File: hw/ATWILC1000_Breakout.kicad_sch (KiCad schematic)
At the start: 1 part, among them IC1 ATWILC1000B-MU-Y

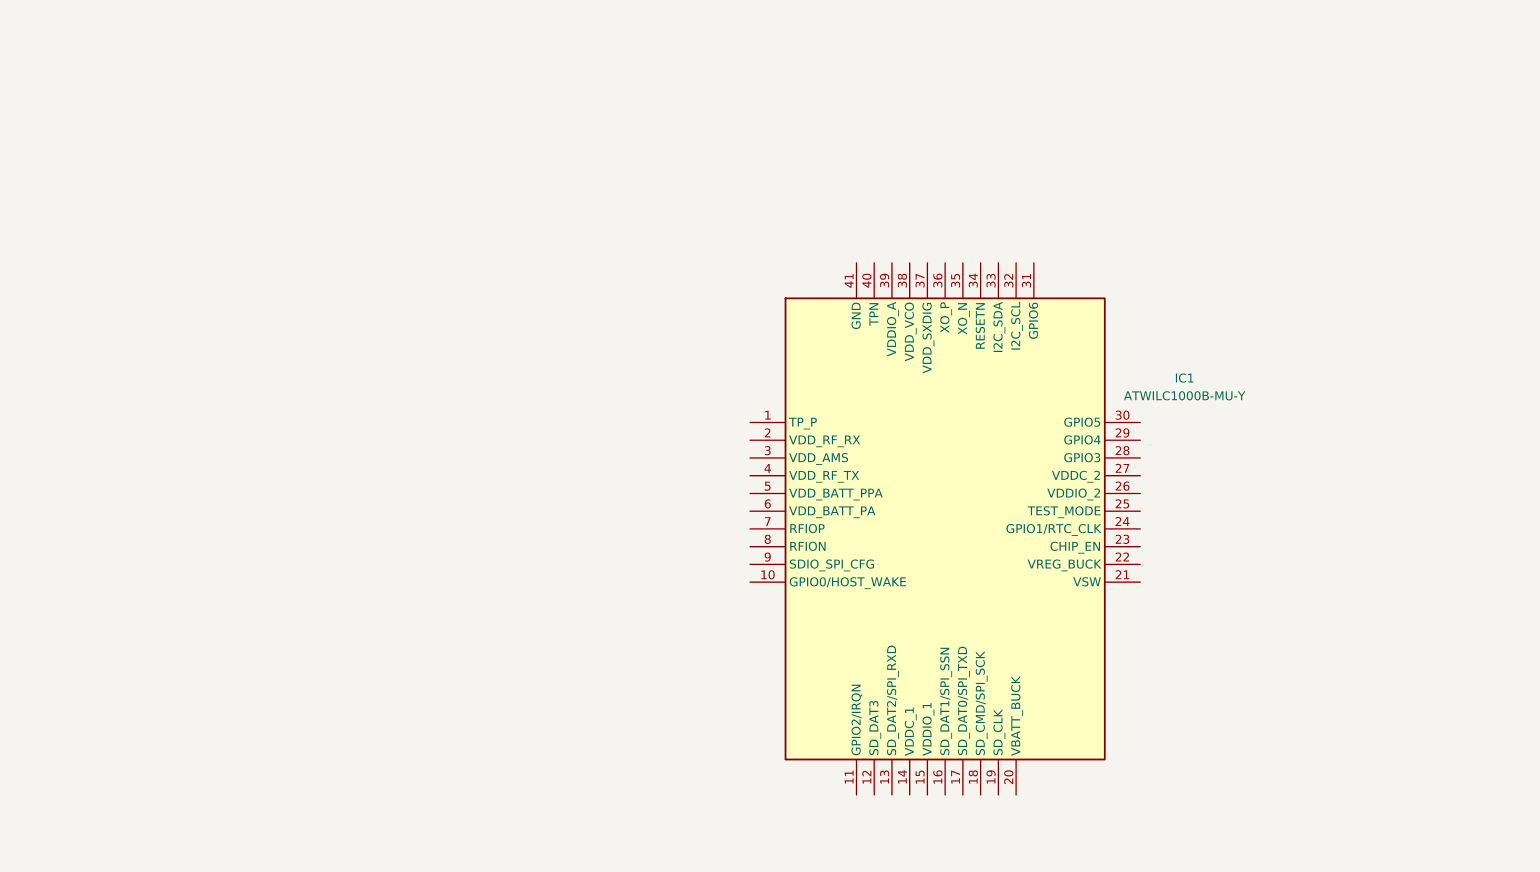
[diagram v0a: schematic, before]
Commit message: started initial power setup for breakout board
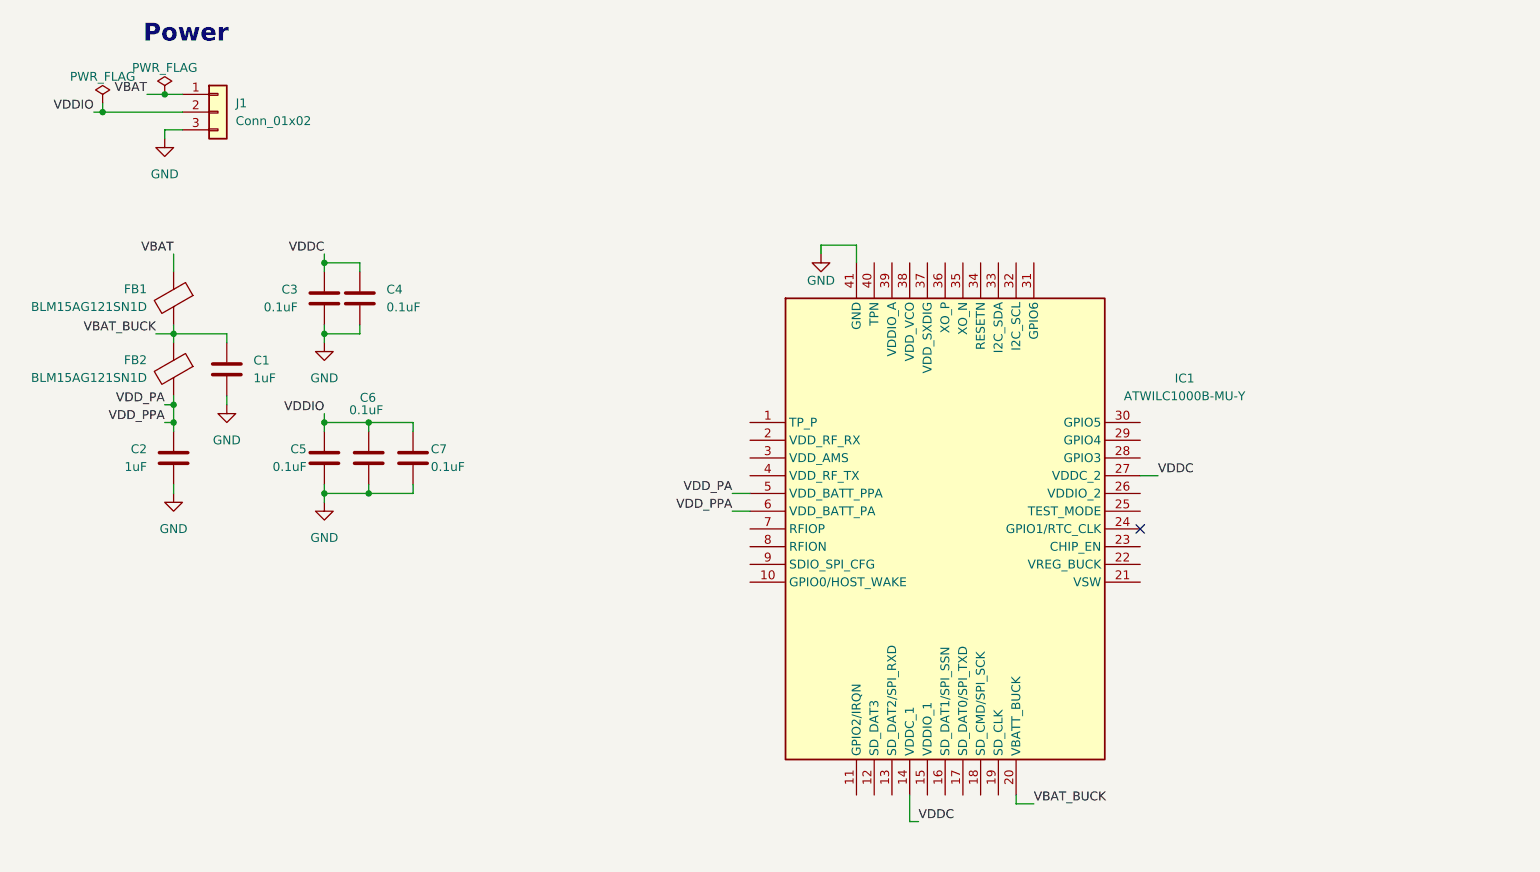
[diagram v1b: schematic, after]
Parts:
- added C1, C2: 1uF, symbol Device:C
- added C3, C4, C5, C6, C7: 0.1uF, symbol Device:C
- added FB1, FB2: BLM15AG121SN1D, symbol Device:FerriteBead
- added J1: Conn_01x02, symbol Connector_Generic:Conn_01x03
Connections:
- net VDDC: now reaches IC1.14 (VDDC_1)
- net VDDC: now also IC1.27 (VDDC_2), C3.1, C4.1
- net VBAT_BUCK: now reaches IC1.20 (VBATT_BUCK)
- net VBAT_BUCK: now also C1.1, FB1.2, FB2.1
- net GND: now reaches IC1.41 (GND)
- net GND: now also C1.2, C2.2, C3.2, C4.2, C5.2, C6.2, C7.2, J1.3 (Pin_3)
- net VDD_PA: now reaches IC1.5 (VDD_BATT_PPA)
- net VDD_PA: now also IC1.6 (VDD_BATT_PA), C2.1, FB2.2
- new net VBAT: FB1.1, J1.1 (Pin_1)
- new net VDDIO: C5.1, C6.1, C7.1, J1.2 (Pin_2)
- no-connect marks 0 -> 1
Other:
- note added: "Power"

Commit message: updated to the module rather than the chip
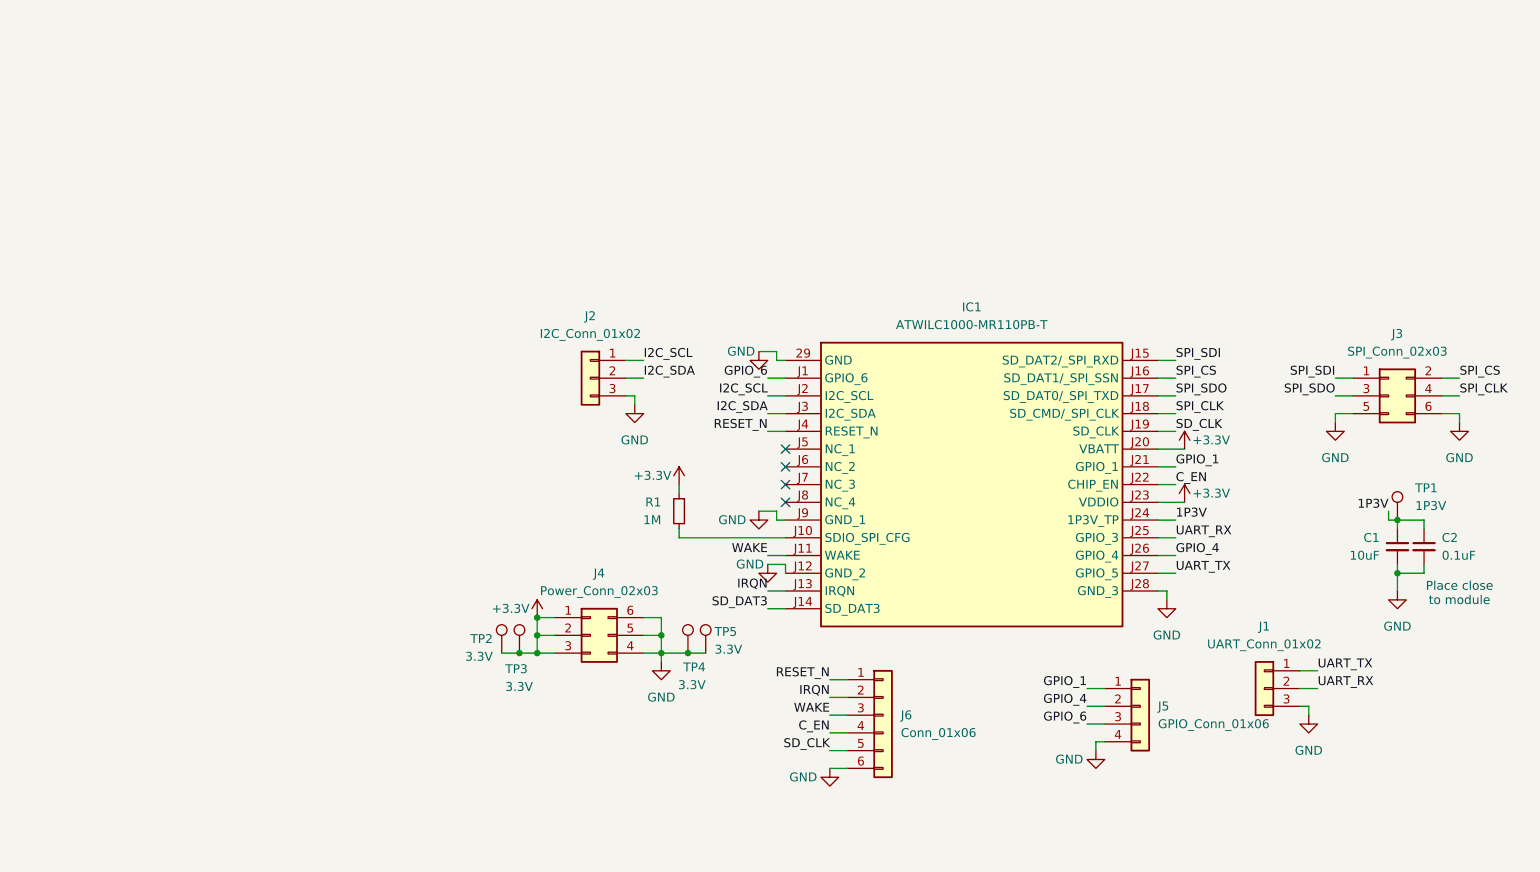
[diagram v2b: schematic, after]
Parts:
- removed C1, C2: 1uF, symbol Device:C
- removed C3, C4, C5, C6, C7: 0.1uF, symbol Device:C
- removed FB1, FB2: BLM15AG121SN1D, symbol Device:FerriteBead
- removed IC1: ATWILC1000B-MU-Y, QFN40P500X500X100-41N-D, symbol ATWILC1000B-MU-Y:ATWILC1000B-MU-Y
- added C1: 10uF, symbol Device:C_Small
- added C2: 0.1uF, symbol Device:C_Small
- added IC1: ATWILC1000-MR110PB-T, ATWILC1000MR110PBT, symbol ATWILC1000-MR110PB-T:ATWILC1000-MR110PB-T
- added J2: I2C_Conn_01x02, symbol Connector_Generic:Conn_01x03
- added J3: SPI_Conn_02x03, symbol Connector_Generic:Conn_02x03_Odd_Even
- added J4: Power_Conn_02x03, symbol Connector_Generic:Conn_02x03_Counter_Clockwise
- added J5: GPIO_Conn_01x06, symbol Connector_Generic:Conn_01x04
- added J6: Conn_01x06, symbol Connector_Generic:Conn_01x06
- added R1: 1M, symbol Device:R_Small
- added TP1: 1P3V, symbol Connector:TestPoint
- added TP2, TP3, TP4, TP5: 3.3V, symbol Connector:TestPoint
- J1: value Conn_01x02 -> UART_Conn_01x02
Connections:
- net GND: now also C1.2, C2.2, IC1.29 (GND), IC1.J12 (GND_2), IC1.J28 (GND_3), IC1.J9 (GND_1), J2.3 (Pin_3), J3.5 (Pin_5), J3.6 (Pin_6), J4.4 (Pin_4), J4.5 (Pin_5), J4.6 (Pin_6), J5.4 (Pin_4), J6.6 (Pin_6), TP4.1, TP5.1
- net VBAT renamed UART_TX
- net UART_TX: now also IC1.J27 (GPIO_5)
- net VDDIO renamed UART_RX
- net UART_RX: now also IC1.J25 (GPIO_3)
- new net: IC1.J10 (SDIO_SPI_CFG), R1.2
- new net +3.3V: IC1.J20 (VBATT), IC1.J23 (VDDIO), J4.1 (Pin_1), J4.2 (Pin_2), J4.3 (Pin_3), R1.1, TP2.1, TP3.1
- new net 1P3V: C1.1, C2.1, IC1.J24 (1P3V_TP), TP1.1
- new net C_EN: IC1.J22 (CHIP_EN), J6.4 (Pin_4)
- new net GPIO_1: IC1.J21 (GPIO_1), J5.1 (Pin_1)
- new net GPIO_4: IC1.J26 (GPIO_4), J5.2 (Pin_2)
- new net GPIO_6: IC1.J1 (GPIO_6), J5.3 (Pin_3)
- new net I2C_SCL: IC1.J2 (I2C_SCL), J2.1 (Pin_1)
- new net I2C_SDA: IC1.J3 (I2C_SDA), J2.2 (Pin_2)
- new net IRQN: IC1.J13 (IRQN), J6.2 (Pin_2)
- new net RESET_N: IC1.J4 (RESET_N), J6.1 (Pin_1)
- new net SD_CLK: IC1.J19 (SD_CLK), J6.5 (Pin_5)
- new net SD_DAT3: IC1.J14 (SD_DAT3)
- new net SPI_CLK: IC1.J18 (SD_CMD/_SPI_CLK), J3.4 (Pin_4)
- new net SPI_CS: IC1.J16 (SD_DAT1/_SPI_SSN), J3.2 (Pin_2)
- new net SPI_SDI: IC1.J15 (SD_DAT2/_SPI_RXD), J3.1 (Pin_1)
- new net SPI_SDO: IC1.J17 (SD_DAT0/_SPI_TXD), J3.3 (Pin_3)
- new net WAKE: IC1.J11 (WAKE), J6.3 (Pin_3)
- no-connect marks 1 -> 4
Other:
- note added: "Place close to module"
- note removed: "Power"

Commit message: breakout layout first draft
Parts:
- removed J4: Power_Conn_02x03, symbol Connector_Generic:Conn_02x03_Counter_Clockwise
- added J1: Conn_02x03_Odd_Even, Connector_PinHeader_2.54mm:PinHeader_2x03_P2.54mm_Vertical, symbol Connector_Generic:Conn_02x03_Odd_Even
- C1, C2: footprint (none) -> Capacitor_SMD:C_0805_2012Metric_Pad1.18x1.45mm_HandSolder
- IC1: footprint ATWILC1000MR110PBT -> LIB_ATWILC1000-MR110PB-T:ATWILC1000MR110PBT
- J2: value I2C_Conn_01x02 -> I2C_Conn_01x03; footprint (none) -> Connector_PinHeader_2.54mm:PinHeader_1x03_P2.54mm_Vertical
- J3: renamed from J6; value Conn_01x06 -> Misc_Conn_02x03; footprint (none) -> Connector_PinHeader_2.54mm:PinHeader_2x03_P2.54mm_Vertical; symbol Connector_Generic:Conn_01x06 -> Connector_Generic:Conn_02x03_Odd_Even
- J4: renamed from J5; value GPIO_Conn_01x06 -> GPIO_Conn_01x04; footprint (none) -> Connector_PinHeader_2.54mm:PinHeader_1x04_P2.54mm_Vertical
- J5: renamed from J1; value UART_Conn_01x02 -> UART_Conn_01x03; footprint (none) -> Connector_PinHeader_2.54mm:PinHeader_1x03_P2.54mm_Vertical
- J6: renamed from J3; value SPI_Conn_02x03 -> SPI_Conn_02x04; footprint (none) -> Connector_PinHeader_2.54mm:PinHeader_2x04_P2.54mm_Vertical; symbol Connector_Generic:Conn_02x03_Odd_Even -> Connector_Generic:Conn_02x04_Odd_Even
- R1: footprint (none) -> Resistor_SMD:R_0805_2012Metric_Pad1.20x1.40mm_HandSolder
- TP1: renamed from TP2; footprint (none) -> TestPoint:TestPoint_Plated_Hole_D3.0mm
- TP2: renamed from TP3; footprint (none) -> TestPoint:TestPoint_Plated_Hole_D3.0mm
- TP3: renamed from TP4; value 3.3V -> GND; footprint (none) -> TestPoint:TestPoint_Plated_Hole_D3.0mm
- TP4: renamed from TP5; value 3.3V -> GND; footprint (none) -> TestPoint:TestPoint_Plated_Hole_D3.0mm
- TP5: renamed from TP1; footprint (none) -> TestPoint:TestPoint_Plated_Hole_D3.0mm
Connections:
- net +3.3V: now also J1.2 (Pin_2), J1.4 (Pin_4), J1.6 (Pin_6)
- net C_EN: now also J3.6 (Pin_6); no longer J3.4 (Pin_4)
- net GND: now also J2.1 (Pin_1), J3.1 (Pin_1), J4.1 (Pin_1), J5.1 (Pin_1), J6.1 (Pin_1), J6.2 (Pin_2), J1.1 (Pin_1), J1.3 (Pin_3), J1.5 (Pin_5); no longer J2.3 (Pin_3), J3.6 (Pin_6), J4.4 (Pin_4), J5.3 (Pin_3), J6.5 (Pin_5), J6.6 (Pin_6)
- net GPIO_1: now also J4.4 (Pin_4); no longer J4.1 (Pin_1)
- net GPIO_4: now also J4.3 (Pin_3); no longer J4.2 (Pin_2)
- net GPIO_6: now also J4.2 (Pin_2); no longer J4.3 (Pin_3)
- net I2C_SCL: now also J2.3 (Pin_3); no longer J2.1 (Pin_1)
- net IRQN: now also J3.4 (Pin_4); no longer J3.2 (Pin_2)
- net RESET_N: now also J3.5 (Pin_5); no longer J3.1 (Pin_1)
- net SD_CLK: now also J6.3 (Pin_3); no longer J3.5 (Pin_5)
- net SD_DAT3: now also J6.8 (Pin_8)
- net SPI_CS: now also J6.6 (Pin_6); no longer J6.2 (Pin_2)
- net SPI_SDI: now also J6.7 (Pin_7); no longer J6.1 (Pin_1)
- net SPI_SDO: now also J6.5 (Pin_5); no longer J6.3 (Pin_3)
- net UART_RX: now also J5.3 (Pin_3); no longer J5.2 (Pin_2)
- net UART_TX: now also J5.2 (Pin_2); no longer J5.1 (Pin_1)
- net WAKE: now also J3.2 (Pin_2); no longer J3.3 (Pin_3)
- no-connect marks 4 -> 5
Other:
- moved on the sheet: J2, J3, J5, TP1, TP2, TP3, TP4

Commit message: finished and ordered board
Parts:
- removed J1: Conn_02x03_Odd_Even, Connector_PinHeader_2.54mm:PinHeader_2x03_P2.54mm_Vertical, symbol Connector_Generic:Conn_02x03_Odd_Even
- removed J4: GPIO_Conn_01x04, Connector_PinHeader_2.54mm:PinHeader_1x04_P2.54mm_Vertical, symbol Connector_Generic:Conn_01x04
- added J1: 3V3_Conn_01x04, Connector_PinHeader_2.54mm:PinHeader_1x04_P2.54mm_Vertical, symbol Connector_Generic:Conn_01x04
- added J2: VBAT_Conn_01x04, Connector_PinHeader_2.54mm:PinHeader_1x04_P2.54mm_Vertical, symbol Connector_Generic:Conn_01x04
- added J5: VBAT_3V3_Jump_Conn_01x02, Connector_PinHeader_2.54mm:PinHeader_1x02_P2.54mm_Vertical, symbol Connector_Generic:Conn_01x02
- added TP3: VBAT, TestPoint:TestPoint_THTPad_1.5x1.5mm_Drill0.7mm, symbol Connector:TestPoint
- J3: renamed from J2; value I2C_Conn_01x03 -> I2C_CEN_Conn_01x04; footprint Connector_PinHeader_2.54mm:PinHeader_1x03_P2.54mm_Vertical -> Connector_PinHeader_2.54mm:PinHeader_1x04_P2.54mm_Vertical; symbol Connector_Generic:Conn_01x03 -> Connector_Generic:Conn_01x04
- J4: renamed from J3; value Misc_Conn_02x03 -> Misc_Conn_01x03; footprint Connector_PinHeader_2.54mm:PinHeader_2x03_P2.54mm_Vertical -> Connector_PinHeader_2.54mm:PinHeader_1x03_P2.54mm_Vertical; symbol Connector_Generic:Conn_02x03_Odd_Even -> Connector_Generic:Conn_01x03
- J6: renamed from J5; value UART_Conn_01x03 -> UART_Conn_01x05; footprint Connector_PinHeader_2.54mm:PinHeader_1x03_P2.54mm_Vertical -> Connector_PinHeader_2.54mm:PinHeader_1x05_P2.54mm_Vertical; symbol Connector_Generic:Conn_01x03 -> Connector_Generic:Conn_01x05
- J7: renamed from J6; value SPI_Conn_02x04 -> SPI_Conn_02x05; footprint Connector_PinHeader_2.54mm:PinHeader_2x04_P2.54mm_Vertical -> Connector_PinHeader_2.54mm:PinHeader_2x05_P2.54mm_Vertical; symbol Connector_Generic:Conn_02x04_Odd_Even -> Connector_Generic:Conn_02x05_Odd_Even
- TP1: footprint TestPoint:TestPoint_Plated_Hole_D3.0mm -> TestPoint:TestPoint_THTPad_1.5x1.5mm_Drill0.7mm
- TP2: renamed from TP4; footprint TestPoint:TestPoint_Plated_Hole_D3.0mm -> TestPoint:TestPoint_THTPad_1.5x1.5mm_Drill0.7mm
- TP4: renamed from TP2; footprint TestPoint:TestPoint_Plated_Hole_D3.0mm -> TestPoint:TestPoint_THTPad_1.5x1.5mm_Drill0.7mm
- TP5: renamed from TP3; footprint TestPoint:TestPoint_Plated_Hole_D3.0mm -> TestPoint:TestPoint_THTPad_1.5x1.5mm_Drill0.7mm
- TP7: renamed from TP5; footprint TestPoint:TestPoint_Plated_Hole_D3.0mm -> TestPoint:TestPoint_THTPad_1.5x1.5mm_Drill0.7mm
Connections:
- net +3.3V: now also J1.1 (Pin_1), J1.2 (Pin_2), J5.2 (Pin_2); no longer IC1.J20 (VBATT)
- net C_EN: now also J7.3 (Pin_3); no longer J4.6 (Pin_6)
- net GND: now also J1.3 (Pin_3), J1.4 (Pin_4), J2.3 (Pin_3), J2.4 (Pin_4)
- net GPIO_1: now also J7.4 (Pin_4)
- net GPIO_4: now also J6.3 (Pin_3)
- net GPIO_6: now also J6.5 (Pin_5)
- net I2C_SCL: now also J3.4 (Pin_4); no longer J3.3 (Pin_3)
- net I2C_SDA: now also J3.3 (Pin_3); no longer J3.2 (Pin_2)
- net IRQN: now also J4.3 (Pin_3); no longer J4.4 (Pin_4)
- net RESET_N: now also J3.2 (Pin_2); no longer J4.5 (Pin_5)
- net SD_CLK: now also J7.5 (Pin_5); no longer J7.3 (Pin_3)
- net SD_DAT3: now also J7.10 (Pin_10); no longer J7.8 (Pin_8)
- net SPI_CLK: now also J7.6 (Pin_6); no longer J7.4 (Pin_4)
- net SPI_CS: now also J7.8 (Pin_8); no longer J7.6 (Pin_6)
- net SPI_SDI: now also J7.9 (Pin_9); no longer J7.7 (Pin_7)
- net SPI_SDO: now also J7.7 (Pin_7); no longer J7.5 (Pin_5)
- net UART_RX: now also J6.2 (Pin_2); no longer J6.3 (Pin_3)
- net UART_TX: now also J6.4 (Pin_4); no longer J6.2 (Pin_2)
- new net VBAT: IC1.J20 (VBATT), J2.1 (Pin_1), J2.2 (Pin_2), J5.1 (Pin_1), TP3.1
- no-connect marks 5 -> 4
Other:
- moved on the sheet: R1, TP1, TP2, TP4, TP5
